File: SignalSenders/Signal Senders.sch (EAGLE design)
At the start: 16 parts, among them IC2 MEGA8-P

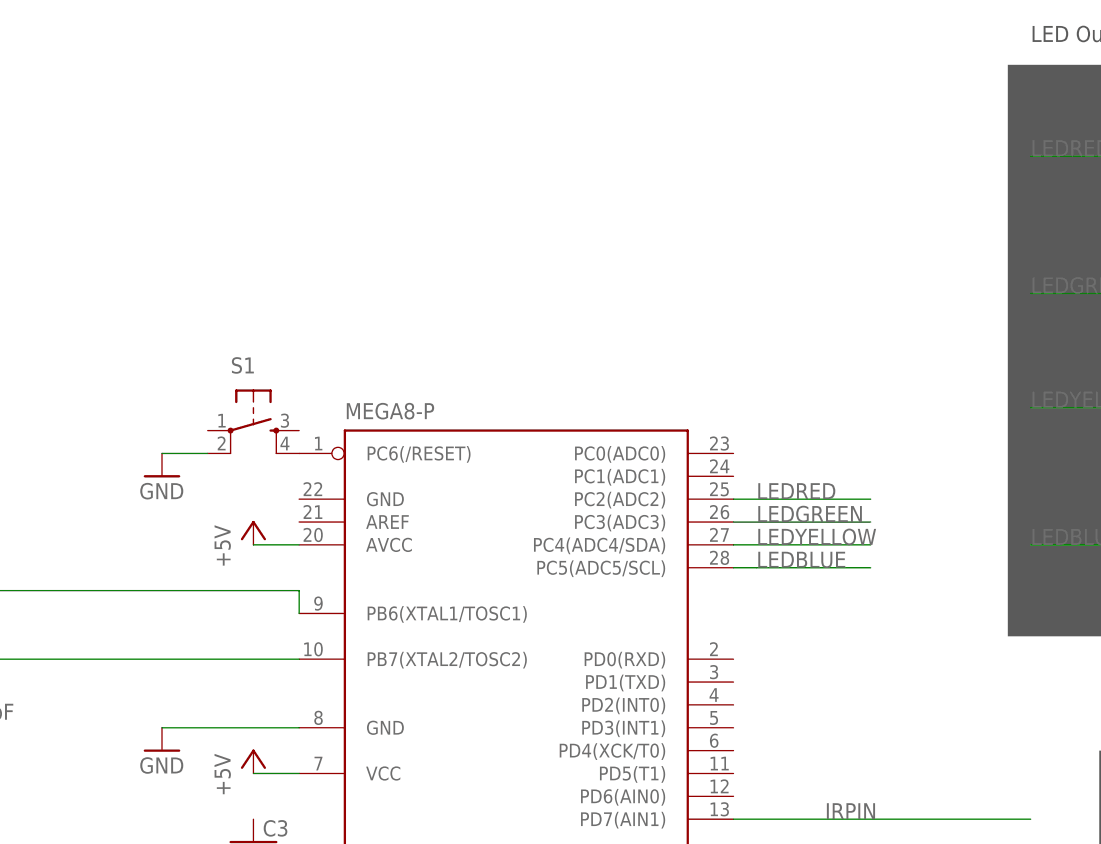
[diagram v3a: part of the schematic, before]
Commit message: EAGLE - add headers for Tx and Rx
Headers to be able to easily program the chip
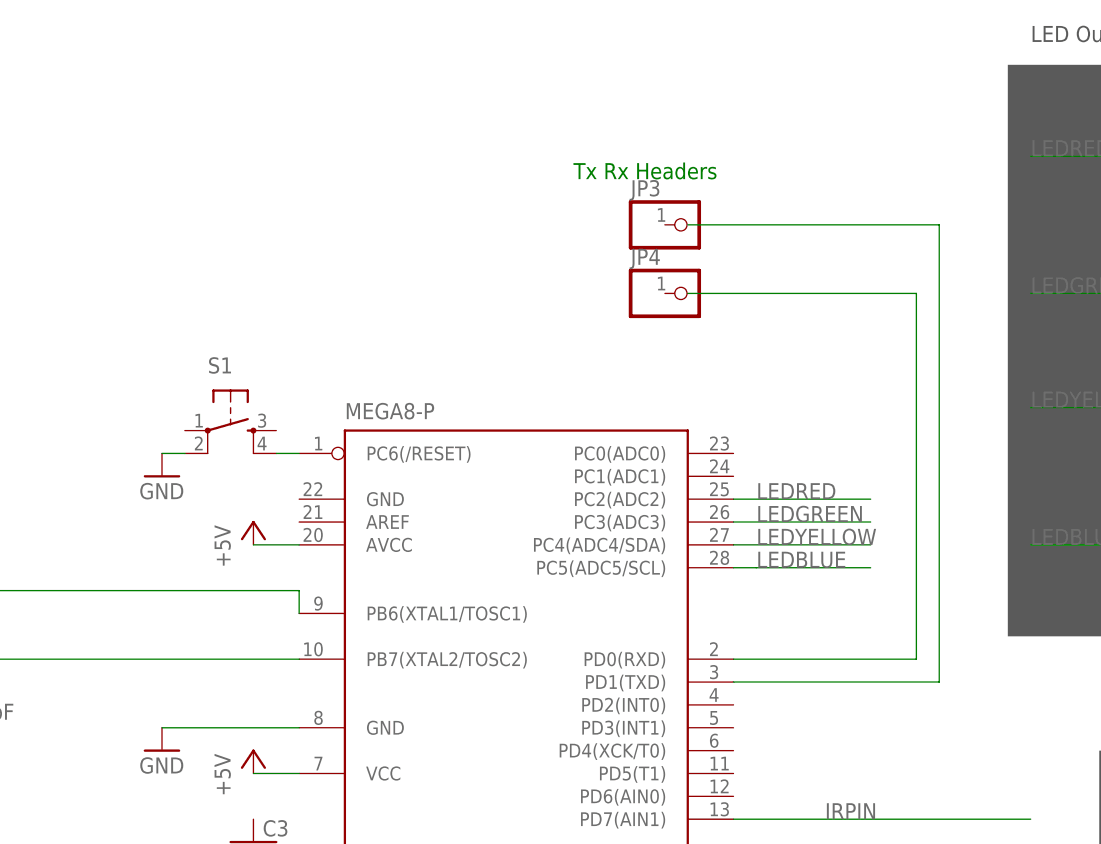
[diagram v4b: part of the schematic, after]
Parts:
- added JP3, JP4: (no value), adafruit:PINHD-1X1
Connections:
- new net N$2: IC2.PD1(TXD)
- new net N$3: IC2.PD0(RXD)
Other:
- note added: "Tx Rx Headers"
- moved on the sheet: S1
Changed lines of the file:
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@@
 <part name="GND10" library="supply1" deviceset="GND" device=""/>
 <part name="C3" library="rcl" deviceset="C-US" device="C0805" value="22pF"/>
+<part name="JP3" library="adafruit" deviceset="PINHD-1X1" device=""/>
+<part name="JP4" library="adafruit" deviceset="PINHD-1X1" device=""/>
 </parts>
 <sheets>
@@
 <rectangle x1="48.26" y1="10.16" x2="73.66" y2="38.1" layer="97"/>
 <text x="55.88" y="40.64" size="1.778" layer="97">IR Sensor</text>
+<text x="157.48" y="101.6" size="1.778" layer="91">Tx Rx Headers</text>
 </plain>
 <instances>
@@
 <instance part="FRAME1" gate="G$1" x="25.4" y="-40.64"/>
 <instance part="Y1" gate="G$1" x="88.9" y="53.34" rot="R90"/>
-<instance part="S1" gate="S" x="121.92" y="73.66"/>
+<instance part="S1" gate="S" x="119.38" y="73.66"/>
 <instance part="GND9" gate="1" x="111.76" y="68.58"/>
 <instance part="GND10" gate="1" x="121.92" y="20.32"/>
 <instance part="C3" gate="G$1" x="121.92" y="27.94"/>
+<instance part="JP3" gate="G$1" x="170.18" y="96.52"/>
+<instance part="JP4" gate="G$1" x="170.18" y="88.9"/>
 </instances>
 <busses>
@@
 <segment>
 <pinref part="S1" gate="S" pin="2"/>
-<wire x1="116.84" y1="71.12" x2="111.76" y2="71.12" width="0.1524" layer="91"/>
+<wire x1="114.3" y1="71.12" x2="111.76" y2="71.12" width="0.1524" layer="91"/>
 <pinref part="GND9" gate="1" pin="GND"/>
 </segment>
@@
 <pinref part="IC2" gate="G$1" pin="PC6(/RESET)"/>
 <pinref part="S1" gate="S" pin="4"/>
+<wire x1="124.46" y1="71.12" x2="127" y2="71.12" width="0.1524" layer="91"/>
 </segment>
 </net>
@@
 </segment>
 </net>
+<net name="N$2" class="0">
+<segment>
+<wire x1="170.18" y1="96.52" x2="198.12" y2="96.52" width="0.1524" layer="91"/>
+<wire x1="198.12" y1="96.52" x2="198.12" y2="45.72" width="0.1524" layer="91"/>
+<pinref part="IC2" gate="G$1" pin="PD1(TXD)"/>
+<wire x1="175.26" y1="45.72" x2="198.12" y2="45.72" width="0.1524" layer="91"/>
+</segment>
+</net>
+<net name="N$3" class="0">
+<segment>
+<wire x1="170.18" y1="88.9" x2="195.58" y2="88.9" width="0.1524" layer="91"/>
+<wire x1="195.58" y1="88.9" x2="195.58" y2="48.26" width="0.1524" layer="91"/>
+<pinref part="IC2" gate="G$1" pin="PD0(RXD)"/>
+<wire x1="175.26" y1="48.26" x2="195.58" y2="48.26" width="0.1524" layer="91"/>
+</segment>
+</net>
